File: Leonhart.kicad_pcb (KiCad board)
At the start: 8 copper layers, 45 x 25 mm, 412 parts, among them J1001 TC2050, J1002 Conn_01x03_Pin, J2001 TC2050, J2002 Conn_01x06_Pin, J2003 SMA-KWE901, J3002 TC2050, J3003 Conn_01x06_Pin, J3004 SMA-KWE901, J7001 USB_C_Receptacle_USB2.0_16P, J7002 USB_A, J7003 Micro_SD_Card_Det1, Q3001 DMG1012T, Q6001 DMG1012T, Q6002 DMG1012T, U1001 AM6231ASGGGAALW, U1002 SN74LVC2G241DCUR, U1003 AT24C32D-STUM-T, U2001 CC2652PSIP, U3001 nRF52840, U4001 TPS6521903RHBR, U4002 TLV62595DMQR, U5001 K4AAG165WA-BCWE, U6001 HR911130A, U6002 RTL8211F-CG, U7001 TVS0500DRVR, U7002 EMMC16G-TB29-PZ90, U7004 TPD3S014, U7005 TPS22918DBVR, X1001 32.768kHz, X1002 25MHz, X3001 32.768kHz, X3002 25MHz, X6001 ECS-2520MV-250-BN-TR

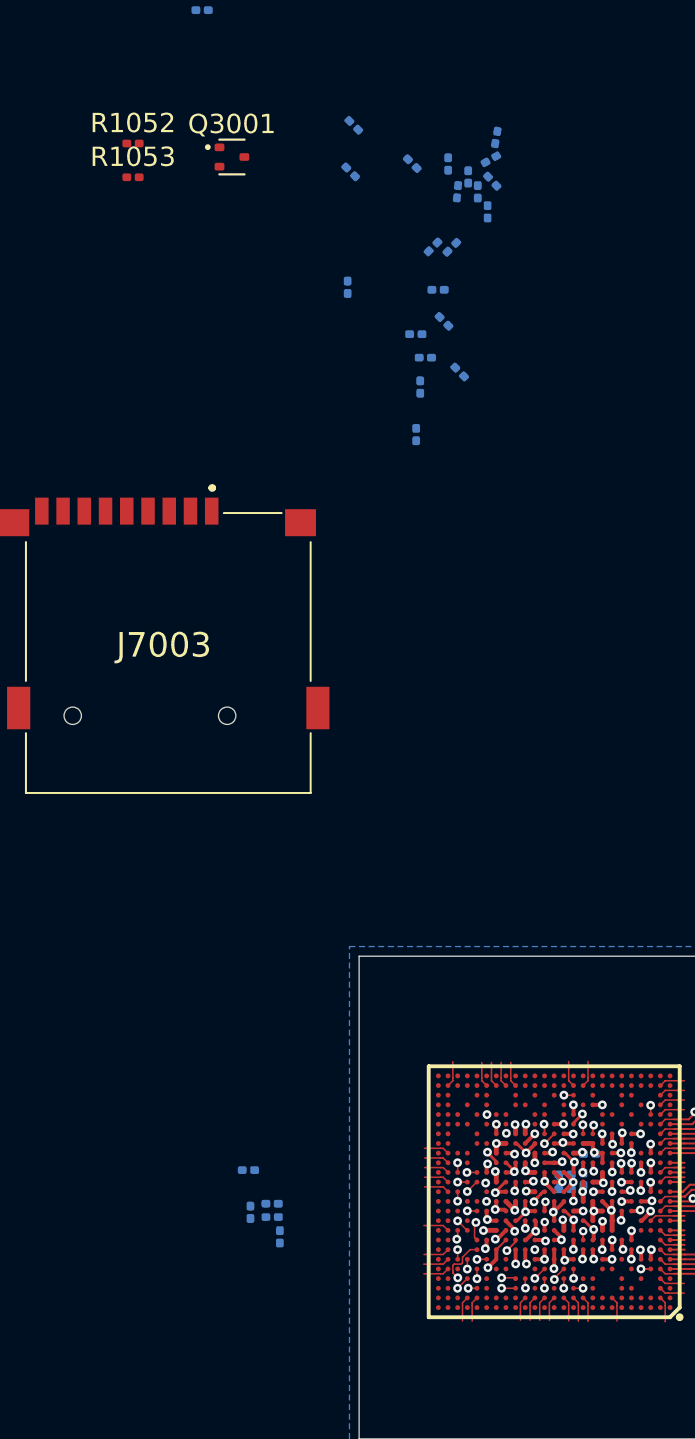
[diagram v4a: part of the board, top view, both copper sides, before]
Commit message: Added more SoC powering decaps
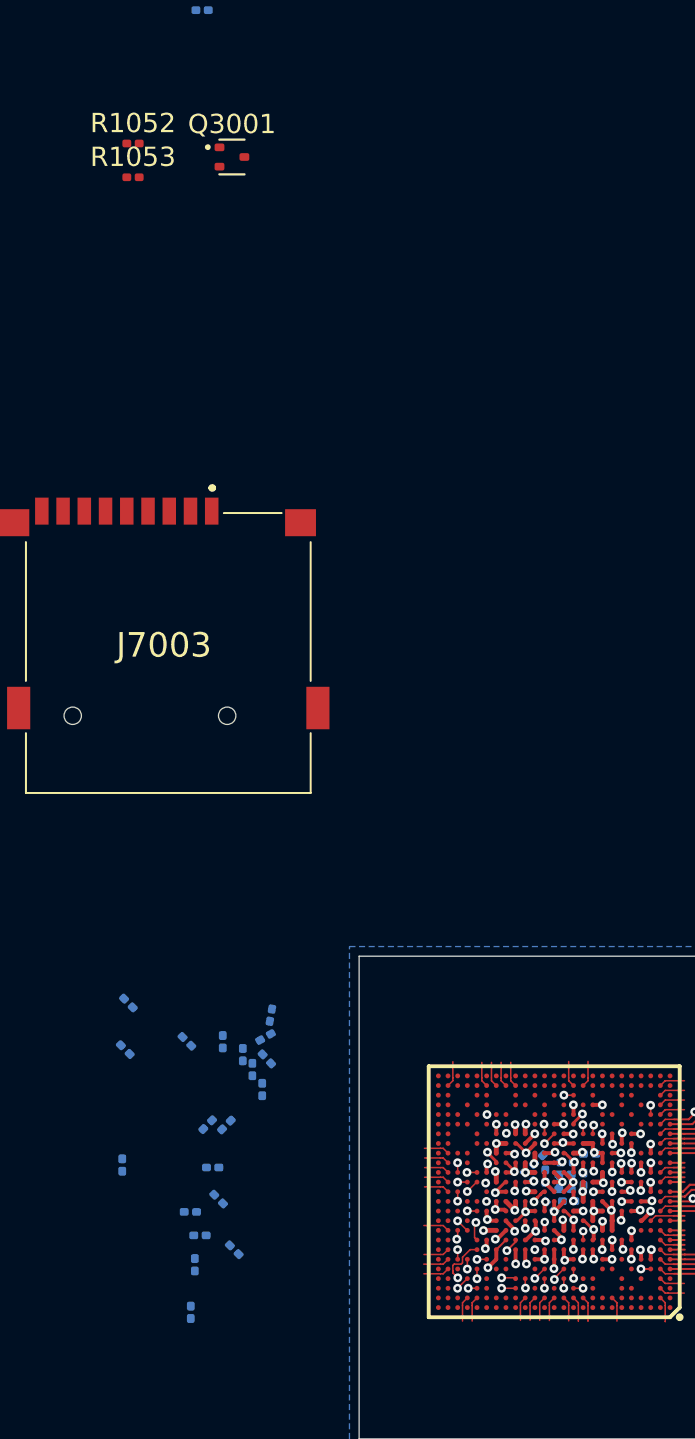
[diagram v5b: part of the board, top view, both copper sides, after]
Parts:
- moved C4054 51.2 mm to (135.9, 182.5), turned to 135 degrees
- moved C4021 46.9 mm to (118.6, 187.0)
- moved C4024 46.9 mm to (120.3, 179.8)
- moved C4026 46.9 mm to (119.9, 183.6)
- moved C4027 46.9 mm to (119.5, 182.0)
- moved C4036 46.9 mm to (121.1, 176.1)
- moved C4037 46.9 mm to (118.2, 175.4)
- moved C4038 46.9 mm to (122.6, 174.1)
- moved C4039 46.9 mm to (121.6, 176.9)
- moved C4055 46.9 mm to (122.4, 176.3)
- moved C4056 46.9 mm to (114.9, 181.8)
- moved C4061 46.9 mm to (118.9, 185.5)
- moved C4062 46.9 mm to (119.3, 179.8)
- moved C4063 46.9 mm to (115.0, 175.9)
- moved C4073 46.9 mm to (120.7, 186.2)
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
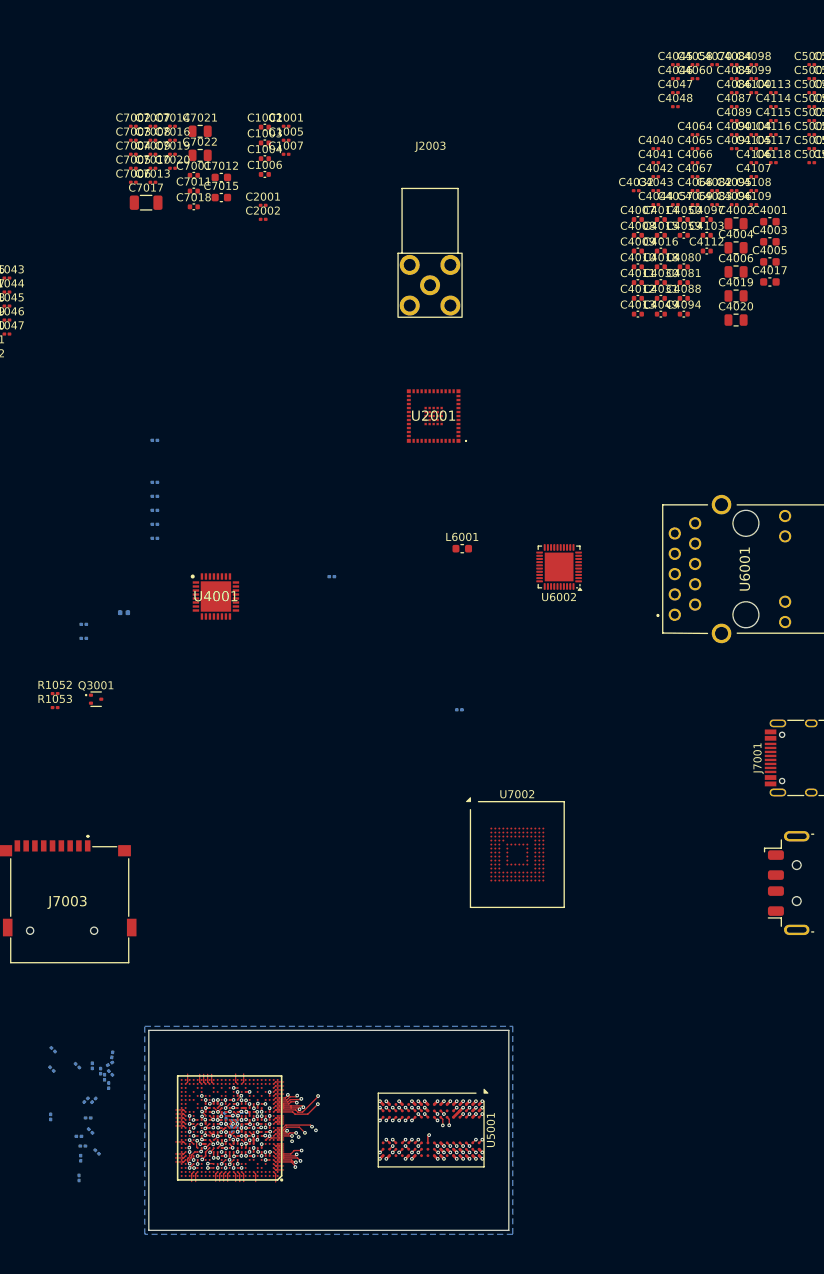
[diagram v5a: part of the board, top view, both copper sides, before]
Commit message: More SoC power decap placement
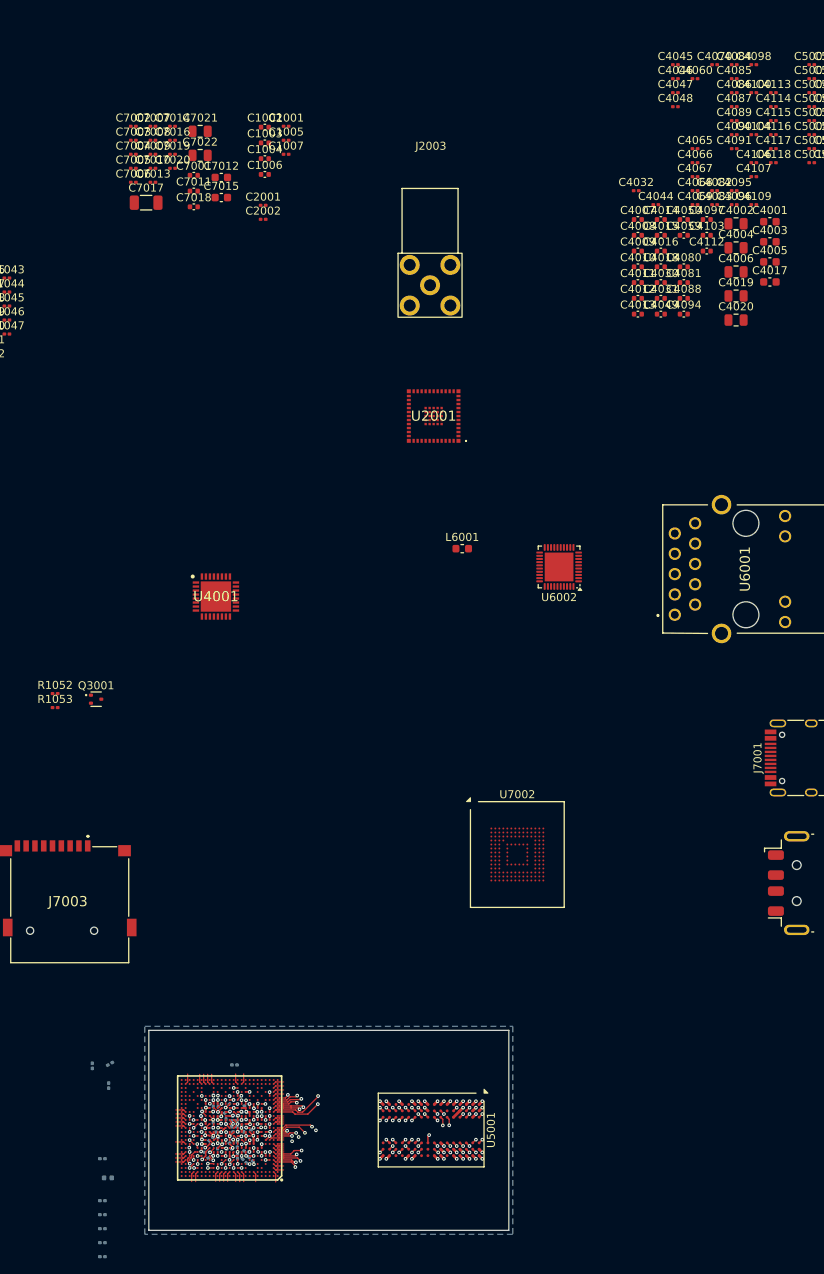
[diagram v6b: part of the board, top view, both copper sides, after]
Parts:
- C4040, C4041, C4042, C4043, C4057, C4058, C4064, C4099, C4105, C4108: moved to B.Cu
- moved C4058 147.8 mm to (135.7, 185.5), turned to -90 degrees
- moved C4064 140.1 mm to (139.1, 187.4), turned to -45 degrees
- moved C4099 139.3 mm to (137.8, 175.3), turned to 180 degrees
- moved C4105 136.5 mm to (137.0, 180.4), turned to 45 degrees
- moved C4108 134.1 mm to (138.8, 184.0), turned to 65 degrees
- moved C4042 132.1 mm to (139.4, 186.2), turned to 170 degrees
- moved C4040 131.9 mm to (135.8, 180.9), turned to 90 degrees
- moved C4041 131.0 mm to (139.6, 183.3), turned to -25 degrees
- moved C4057 129.6 mm to (137.4, 184.9), turned to -135 degrees
- moved C4043 125.2 mm to (139.4, 180.4), turned to -160 degrees
- moved C4072 90.0 mm to (121.3, 187.1)
- moved C4075 90.0 mm to (121.3, 192.3)
- moved C4076 90.0 mm to (121.3, 194.1)
- moved C4077 90.0 mm to (121.3, 195.8)
- moved C4078 90.0 mm to (121.3, 197.6)
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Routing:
- net GND: track 39.0 -> 40.0 mm, vias 50 -> 55
- net /USB and SD [7]/USB1_DRVVBUS: track 0.00 -> 0.73 mm, vias 0 -> 1
- net VDD_1V8: track 6.37 -> 6.91 mm
